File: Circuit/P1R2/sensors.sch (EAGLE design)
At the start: 53 parts, among them IC1 LM2936MP-3.3, Y1 16 Mhz, Y2 16 Mhz

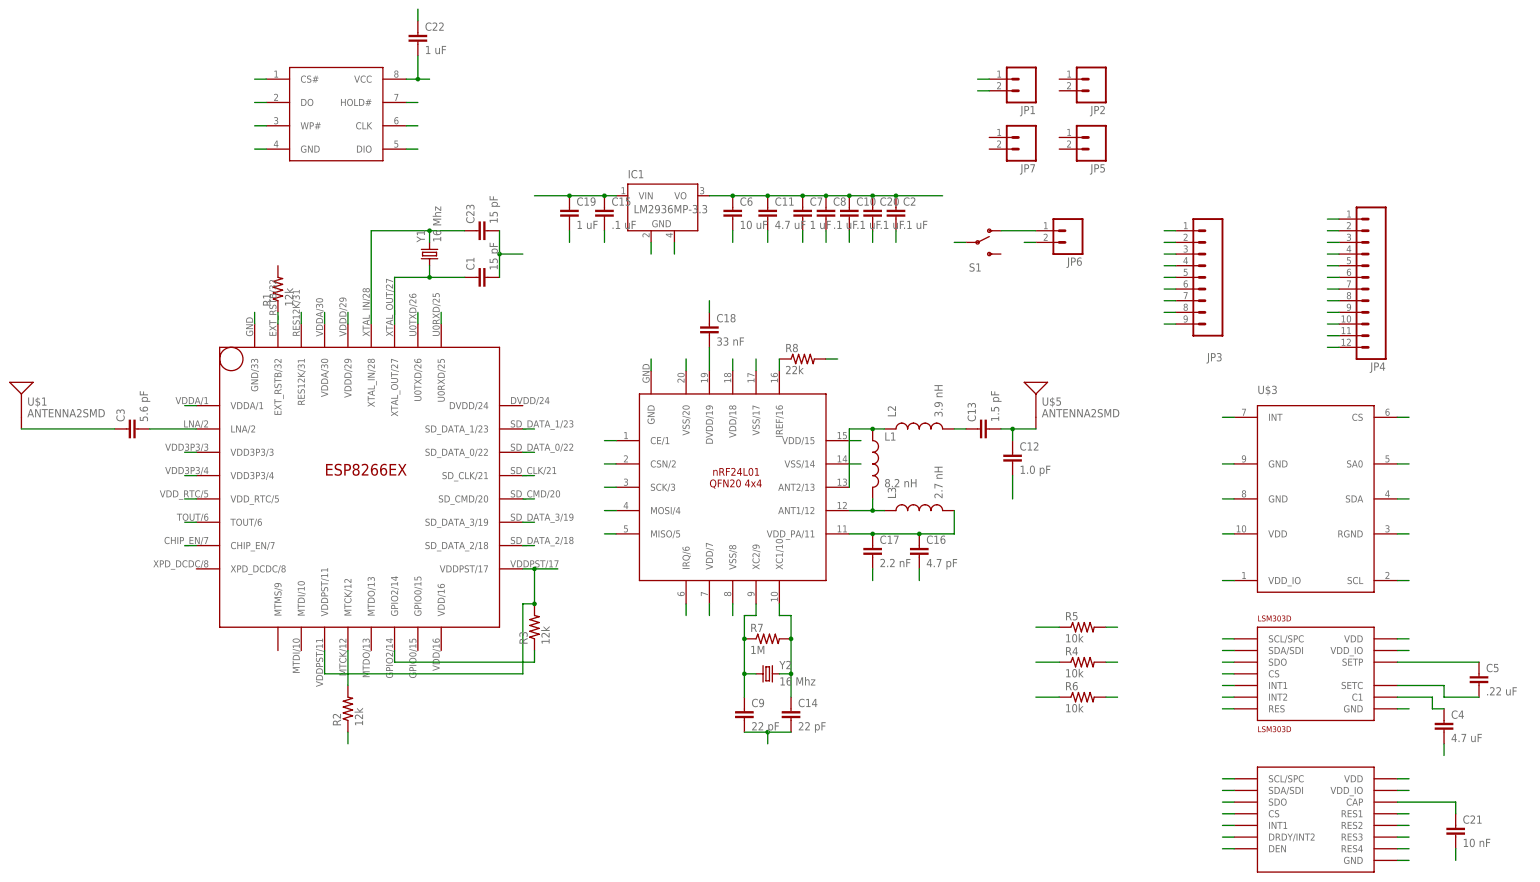
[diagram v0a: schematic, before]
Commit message: Forum boards done
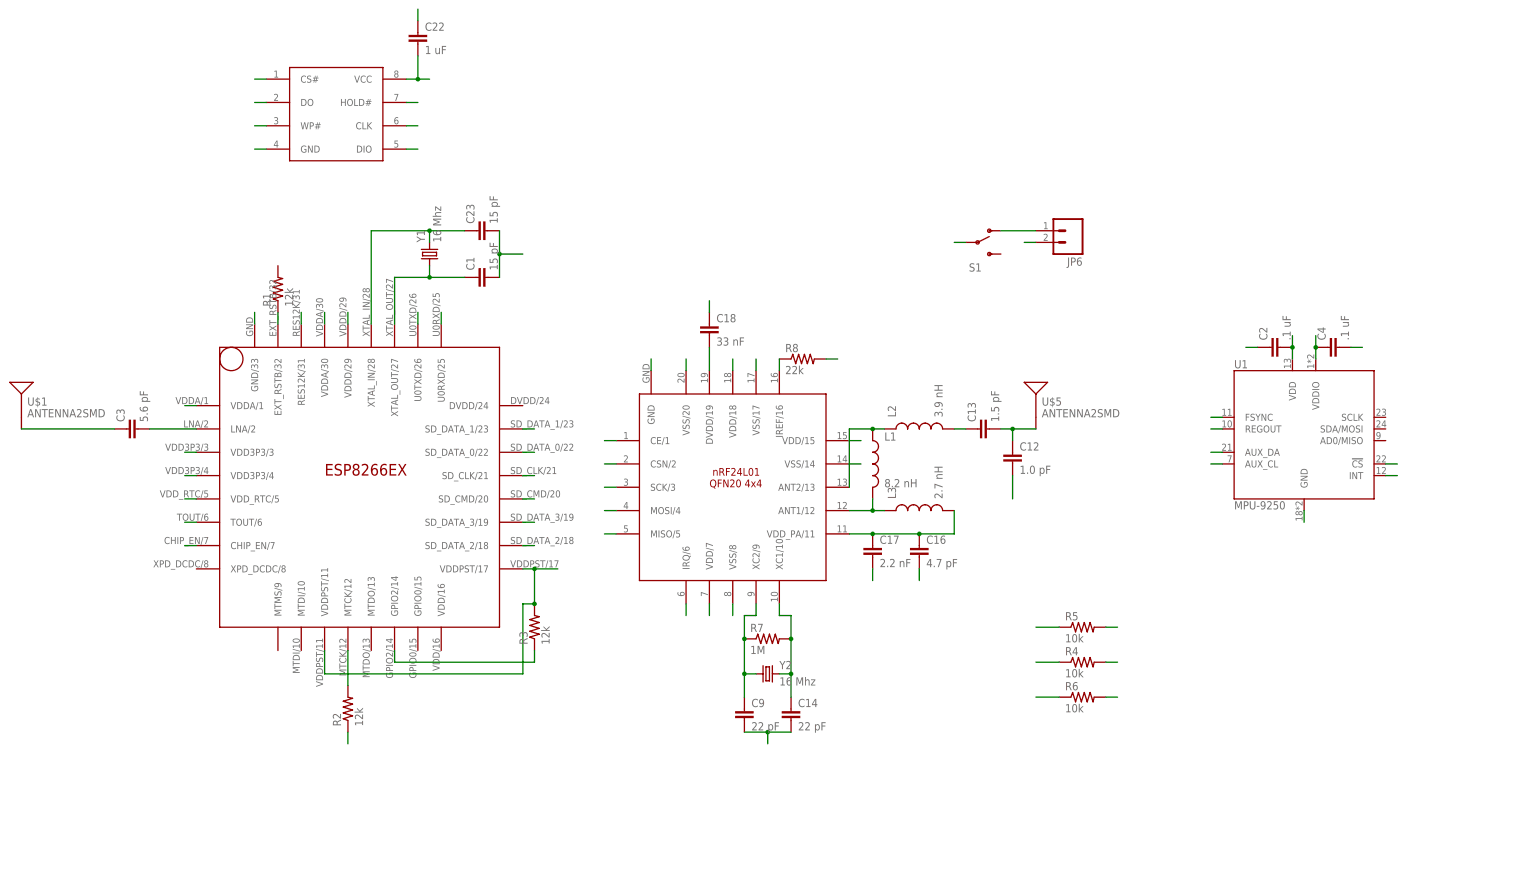
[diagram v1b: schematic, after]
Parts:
- removed C10, C15, C20, C8: .1 uF, SparkFun-Capacitors:CAP0603-CAP
- removed C11: 4.7 uF, SparkFun-Capacitors:CAP0603-CAP
- removed C19, C7: 1 uF, SparkFun-Capacitors:CAP0603-CAP
- removed C21: 10 nF, SparkFun-Capacitors:CAP0603-CAP
- removed C5: .22 uF, SparkFun-Capacitors:CAP0603-CAP
- removed C6: 10 uF, SparkFun-Capacitors:CAP0603-CAP
- removed IC1: LM2936MP-3.3, national-semiconductor:LM2936MP-3.3
- removed JP1, JP2, JP5, JP7: (no value), SparkFun-Connectors:M02LOCK
- removed JP3: (no value), SparkFun-Connectors:M09
- removed JP4: (no value), SparkFun-Connectors:M12PTH
- removed LSM303D: LSM303D, st:LSM303D
- removed U$3: LPS25H, chips:LPS25H
- removed U$4: L3GD20H, st:L3GD20H
- added U1: MPU-9250, chips:MPU-9250
- C4: value 4.7 uF -> .1 uF
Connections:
- net VIN renamed VCC
- removed net N$22: C21.1, U$4.CAP
- removed net N$31: C21.2
- removed net N$35: LSM303D.INT1
- removed net N$36: LSM303D.INT2
- removed net N$42: C5.2, LSM303D.SETC
- removed net N$43: C4.1, LSM303D.C1
- removed net SETP: C5.1, LSM303D.SETP
- new net 3.3V: C2.2, C22.2, C4.1, MESH.VDD/15, MESH.VDD/18, MESH.VDD/7, R3.2, U$2.VCC, U1.VDD, U1.VDDIO, WIFI.CHIP_EN/7, WIFI.VDD3P3/3, WIFI.VDD3P3/4, WIFI.VDDA/1, WIFI.VDDD/29, WIFI.VDDPST/11, WIFI.VDDPST/17
- new net N$4: U1.FSYNC
- new net N$7: U1.REGOUT
- new net N$8: U1.AUX_DA
- new net N$9: U1.AUX_CL
- net CE: no longer JP3.3
- net CSN: no longer JP3.4
- net GND: now also C2.1; no longer C10.2, C11.2, C15.2, C19.2, C2.2, C20.2, C6.2, C7.2, C8.2, IC1.GND@1, IC1.GND@2, JP1.2, JP4.1, JP4.2, JP4.3, JP4.4, JP4.5, JP4.6, LSM303D.GND, LSM303D.RES, U$3.GND@1, U$3.GND@2, U$3.RGND, U$4.DEN, U$4.GND, U$4.RES1, U$4.RES2, U$4.RES3
- net MISO: no longer JP3.6
- net MOSI: no longer JP3.5
- net N$11: now also U1.GND; no longer U$4.INT1
- net N$12: now also U1.INT; no longer U$4.DRDY/INT2
- net N$14: now also U1.!CS; no longer U$3.INT
- net RX_W: no longer JP3.1
- net SCK: no longer JP3.7
- net SCL: no longer JP3.9, LSM303D.SCL/SPC, U$3.SCL, U$4.SCL/SPC
- net SDA: no longer JP3.8, LSM303D.SDA/SDI, U$3.SDA, U$4.SDA/SDI
- net SDO: no longer LSM303D.SDO, U$3.SA0, U$4.SDO
- net TX_W: no longer JP3.2
- net VDD: no longer C10.1, C11.1, C2.1, C20.1, C22.2, C6.1, C7.1, C8.1, IC1.VO, JP1.1, JP4.10, JP4.11, JP4.12, JP4.7, JP4.8, JP4.9, LSM303D.CS, LSM303D.VDD, LSM303D.VDD_IO, MESH.VDD/15, MESH.VDD/18, MESH.VDD/7, R3.2, U$2.VCC, U$3.CS, U$3.VDD, U$3.VDD_IO, U$4.CS, U$4.RES4, U$4.VDD, U$4.VDD_IO, WIFI.CHIP_EN/7, WIFI.VDD3P3/3, WIFI.VDD3P3/4, WIFI.VDDA/1, WIFI.VDDD/29, WIFI.VDDPST/11, WIFI.VDDPST/17
- net VRAW: no longer C15.1, C19.1, IC1.VIN
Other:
- moved on the sheet: C2, C4
